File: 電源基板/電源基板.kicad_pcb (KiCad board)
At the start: 2 copper layers, 59.7 x 49.5 mm, 22 parts, among them J1 XT30, J2 PWR out, J3 Power Switch, J4 5V out, Q2 Q_NMOS_GDS, U1 OKL-T/6-W12N-C

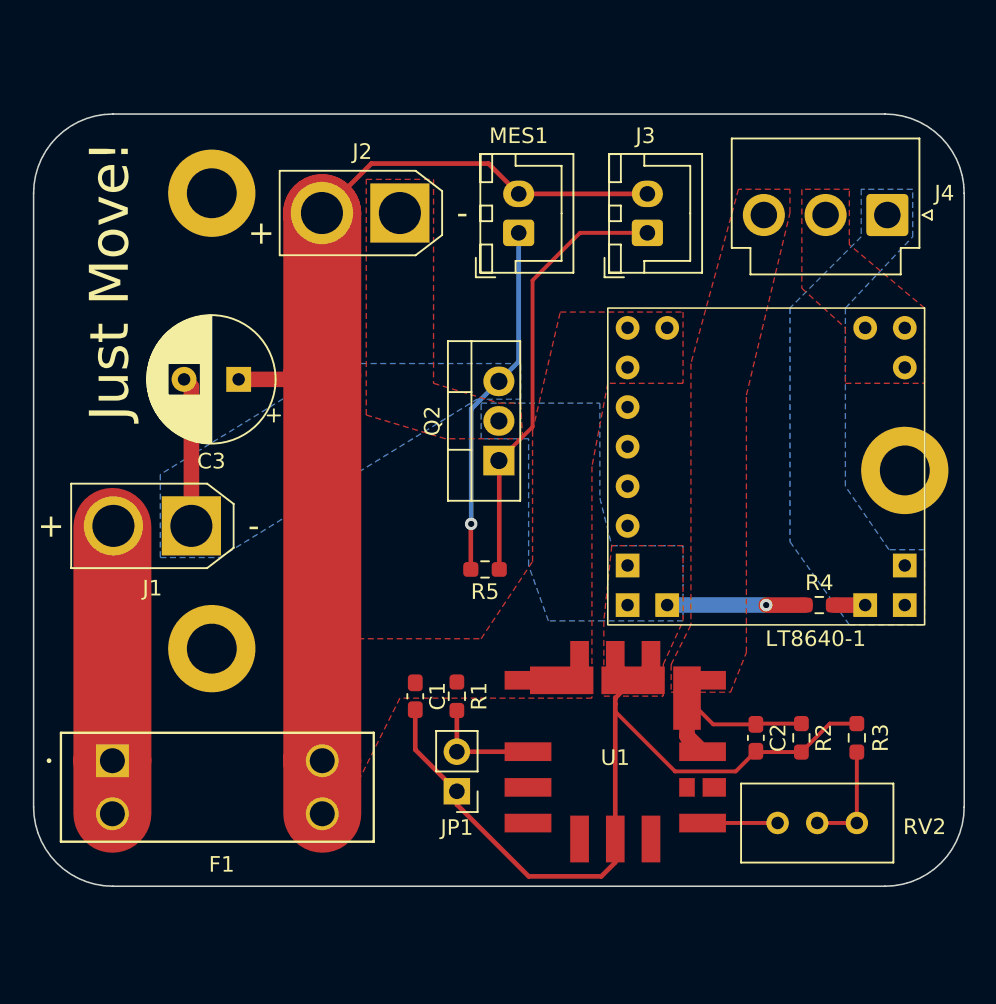
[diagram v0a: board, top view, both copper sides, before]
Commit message: パスコンと保護ダイオードの追加
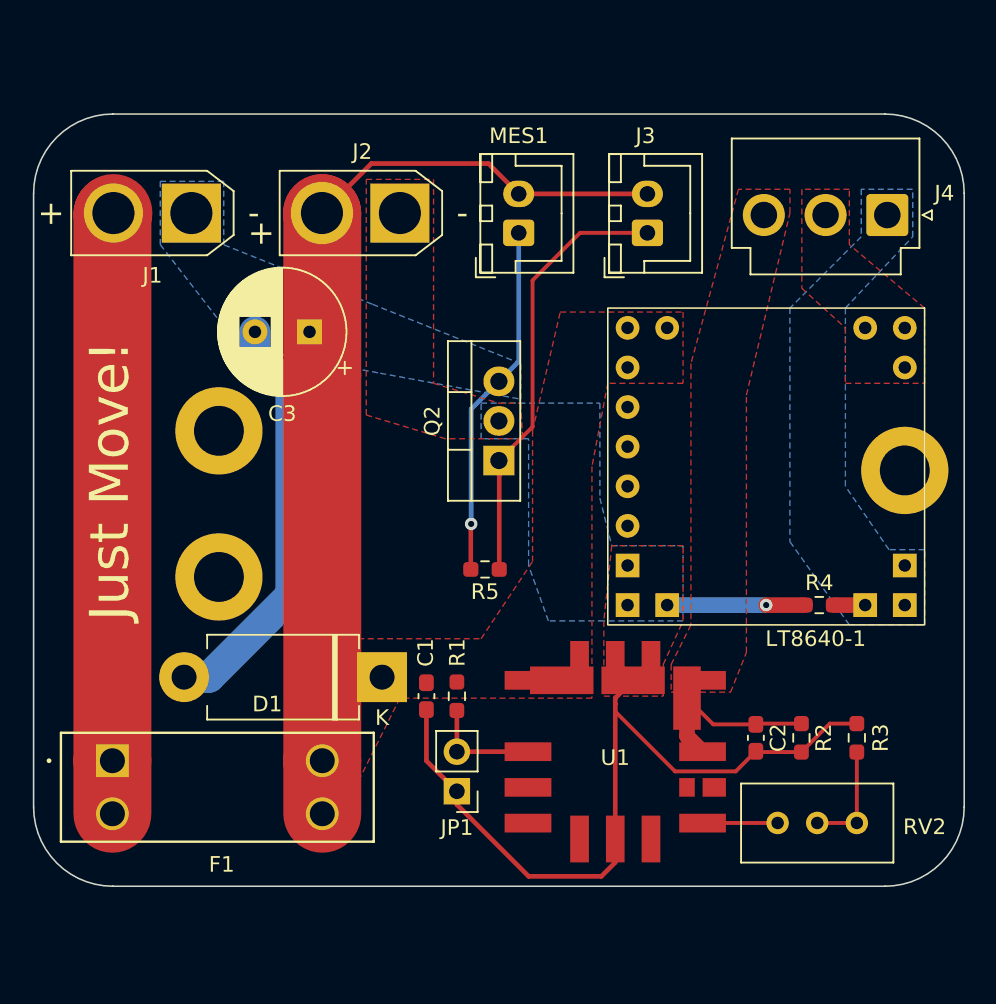
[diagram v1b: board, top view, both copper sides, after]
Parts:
- added D1: D_Shockley, Diode_THT:D_DO-201AD_P12.70mm_Horizontal, F.Cu at (52.8, 122.5)
- moved J1 20.1 mm to (40.6, 92.7)
- moved REF** 15.2 mm to (42.4, 106.7)
- moved C3 5.47 mm to (48.2, 100.3)
- moved REF** 4.62 mm to (42.4, 116.1)
- moved C1 0.71 mm to (55.7, 123.7)
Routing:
- net Net-(J1-Pin_2): track 18.6 -> 38.7 mm
- net GND: track 32.5 -> 49.7 mm
- net VDD: track 67.0 -> 61.5 mm

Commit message: サーボ基板
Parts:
- added J5: Conn_01x02_Pin, Connector_PinHeader_2.54mm:PinHeader_1x02_P2.54mm_Vertical, F.Cu at (53.0, 117.5)
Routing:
- net GND2: track 61.4 -> 77.2 mm

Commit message: 電源基板
白色にして発注
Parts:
- removed C1: 22u, Capacitor_SMD:C_0603_1608Metric_Pad1.08x0.95mm_HandSolder
- removed C2: 10u, Capacitor_SMD:C_0603_1608Metric_Pad1.08x0.95mm_HandSolder
- removed J5: Conn_01x02_Pin, Connector_PinHeader_2.54mm:PinHeader_1x02_P2.54mm_Vertical
- removed JP1: JumperShort, Connector_PinHeader_2.54mm:PinHeader_1x02_P2.54mm_Vertical
- removed R4: R_Small, Resistor_SMD:R_0603_1608Metric_Pad0.98x0.95mm_HandSolder
- removed the REF** at (42.4, 106.7)
- removed the REF** at (42.4, 116.1)
- removed the REF** at (86.4, 109.2)
- removed RV2: 20k, Potentiometer_THT:Potentiometer_Bourns_3296W_Vertical
- added D3: RED, LED_THT:LED_D5.0mm_Horizontal_O3.81mm_Z3.0mm, F.Cu at (79.8, 128.9)
- added FAN1: Conn_01x02_Pin, Connector_PinHeader_2.54mm:PinHeader_1x02_P2.54mm_Vertical, F.Cu at (65.2, 129.0)
- added G***: LOGO, logo:logo2, F.Cu at (33.0, 110.7)
- added LT8640-2: ~, LT8640:LT8640, F.Cu at (78.7, 122.7)
- added LT8640-3: ~, LT8640:LT8640, F.Cu at (78.7, 101.0)
- added REF**: MountingHole_2.2mm_M2_DIN965_Pad, MountingHole:MountingHole_2.2mm_M2_DIN965_Pad, F.Cu at (80.0, 101.0)
- added REF**: MountingHole_2.2mm_M2_DIN965_Pad, MountingHole:MountingHole_2.2mm_M2_DIN965_Pad, F.Cu at (80.3, 125.0)
- added REF**: MountingHole_2.2mm_M2_DIN965_Pad, MountingHole:MountingHole_2.2mm_M2_DIN965_Pad, F.Cu at (50.8, 107.3)
- J2: value PWR out -> Conn_01x02_Pin; footprint Connector_AMASS:AMASS_XT30U-F_1x02_P5.0mm_Vertical -> Connector_PinHeader_2.54mm:PinHeader_1x02_P2.54mm_Vertical
- J4: value 5V out -> PWR OUT; footprint Connector_JST:JST_VH_B3P-VH_1x03_P3.96mm_Vertical -> Connector_JST:JST_VH_B5P-VH_1x05_P3.96mm_Vertical
- R1: value 20k -> 220
- R2, R3: value 1.2k -> R_Small
- U1: value OKL-T/6-W12N-C -> ATtiny85-20P; footprint OKL-T_6-W12N-C:DCDC-murata-6A -> Package_DIP:DIP-8_W7.62mm
- moved MES1 37.0 mm to (59.8, 130.9), turned to 180 degrees
- moved R3 33.2 mm to (53.1, 112.7), turned to -90 degrees
- moved R2 31.7 mm to (51.2, 112.7), turned to 90 degrees
- moved J3 30.5 mm to (43.1, 108.7), turned to 180 degrees
- moved J2 30.0 mm to (57.1, 122.6), turned to 90 degrees
- moved U1 29.1 mm to (55.6, 104.9)
- moved R5 22.0 mm to (43.2, 100.7), turned to 90 degrees
- moved Q2 20.9 mm to (40.6, 101.6)
- moved LT8640-1 20.3 mm to (57.1, 109.9), turned to 180 degrees
- moved J4 20.3 mm to (64.9, 92.6)
- moved C3 16.4 mm to (44.0, 116.2)
- moved R1 7.65 mm to (65.3, 123.4), turned to 180 degrees
- moved J1 2.16 mm to (40.6, 90.6)
- moved D1 1.40 mm to (52.5, 123.8)
- moved F1 1.02 mm to (35.5, 128.9)
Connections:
- J2 pad 1: GND2 -> GND3
- J2 pad 2: VDD -> /tx
- J4 pad 1: GND2 -> GND3
- J4 pad 2: +5VA -> +5V
- J4 pad 3: +5VD -> GND1
- LT8640-1 pad 11: +5VA -> /6VA
- LT8640-1 pad 12: +5VA -> /6VA
- LT8640-1 pad 13: +5VA -> /6VA
- LT8640-1 pad 14: GND2 -> GND1
- LT8640-1 pad 15: GND2 -> GND1
- LT8640-1 pad 16: GND2 -> GND1
- LT8640-1 pad 4: unconnected-(LT8640-1-EN/UV-Pad4) -> /init_6v
- R1 pad 1: VDD -> Net-(D3-K)
- R1 pad 2: Net-(JP1-B) -> GND3
- R2 pad 1: +5VD -> VDD
- R2 pad 2: GND2 -> /Vref
- R3 pad 1: Net-(R3-Pad1) -> /Vref
- R3 pad 2: GND2 -> GND3
- U1 pad 1: Net-(JP1-B) -> unconnected-(U1-~{RESET}/PB5-Pad1)
- U1 pad 2: VDD -> /led
- U1 pad 3: GND2 -> /tx
- U1 pad 4: +5VD -> GND3
- U1 pad 5: +5VD -> /init_6v
- U1 pad 6: Net-(U1-TRIM1) -> /init_5v
- U1 pad 7: GND2 -> /Vref
- U1 pad 8: unconnected-(U1-NC-Pad8) -> +5V
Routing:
- net VDD: track 61.5 -> 152.4 mm
- net GND3: track 0.00 -> 78.0 mm, vias 0 -> 3
- net /6VB: track 0.00 -> 63.1 mm
- net /init_6v: track 0.00 -> 52.9 mm
- net GND1: track 0.00 -> 40.6 mm
- net /led: track 0.00 -> 38.9 mm, vias 0 -> 1
- net +5V: track 0.00 -> 36.4 mm
- net GND: track 49.7 -> 80.3 mm, vias 1 -> 0
- net /init_5v: track 0.00 -> 27.3 mm, vias 0 -> 1
- net Net-(J3-Pin_1): track 28.1 -> 10.7 mm
- net /6VA: track 0.00 -> 17.4 mm
- net Net-(D3-K): track 0.00 -> 15.8 mm
- net /Vref: track 0.00 -> 14.5 mm
- net /tx: track 0.00 -> 14.2 mm, vias 0 -> 2
- net +5VD: track 11.9 -> 0.00 mm
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- removed copper zone on F.Cu, net +5VA
- removed copper zone on F.Cu, net +5VD
- removed copper zone on B.Cu, net GND
- removed copper zone on F.Cu, net GND2
- removed copper zone on F.Cu, net VDD
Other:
- board text removed: "Just Move!"

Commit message: main
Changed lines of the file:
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@@
 		(tags "THT DIP DIL PDIP 2.54mm 7.62mm 300mil")
 		(property "Reference" "U1"
-			(at 3.8 10.15 360)
+			(at 3.8 10.15 0)
 			(layer "F.SilkS")
 			(effects
@@
 		)
 		(property "Value" "ATtiny85-20P"
-			(at 3.81 9.95 360)
+			(at 3.81 9.95 0)
 			(layer "F.Fab")
 			(effects
@@
 		)
 		(fp_text user "${REFERENCE}"
-			(at 3.81 3.81 360)
+			(at 3.81 3.81 0)
 			(layer "F.Fab")
 			(effects
@@
 		(tags "Diode DO-201AD series Axial Horizontal pin pitch 12.7mm  length 9.5mm diameter 5.2mm")
 		(property "Reference" "D1"
-			(at 6.223 3.429 360)
+			(at 6.223 3.429 0)
 			(layer "F.SilkS")
 			(effects
@@
 		)
 		(property "Value" "D_Shockley"
-			(at 6.35 3.72 360)
+			(at 6.35 3.72 0)
 			(layer "F.Fab")
 			(effects
@@
 		)
 		(fp_text user "K"
-			(at 0 -2.6 360)
+			(at 0 -2.6 0)
 			(layer "F.SilkS")
 			(effects
@@
 		)
 		(fp_text user "K"
-			(at 0 -2.6 360)
+			(at 0 -2.6 0)
 			(layer "F.Fab")
 			(effects
@@
 		)
 		(fp_text user "${REFERENCE}"
-			(at 7.0625 0 360)
+			(at 7.0625 0 0)
 			(layer "F.Fab")
 			(effects
@@
 		)
 		(property "Value" "Power Switch"
-			(at 1.25 4.6 360)
+			(at 1.25 4.6 0)
 			(layer "F.Fab")
 			(effects
@@
 		)
 		(fp_text user "${REFERENCE}"
-			(at 1.25 2.7 360)
+			(at 1.25 2.7 0)
 			(layer "F.Fab")
 			(effects
@@
 		)
 		(property "Value" "Voltmeter_DC_XH"
-			(at 1.25 4.6 360)
+			(at 1.25 4.6 0)
 			(layer "F.Fab")
 			(effects
@@
 		)
 		(fp_text user "${REFERENCE}"
-			(at 1.25 2.7 360)
+			(at 1.25 2.7 0)
 			(layer "F.Fab")
 			(effects
@@
 		(tags "resistor handsolder")
 		(property "Reference" "R1"
-			(at 0 -1.43 360)
+			(at 0 -1.43 0)
 			(layer "F.SilkS")
 			(effects
@@
 		)
 		(property "Value" "220"
-			(at 0 1.43 360)
+			(at 0 1.43 0)
 			(layer "F.Fab")
 			(effects
@@
 		)
 		(fp_text user "${REFERENCE}"
-			(at 0 0 360)
+			(at 0 0 0)
 			(layer "F.Fab")
 			(effects
@@
 		)
 		(property "Value" "1000u"
-			(at 1.75 5.25 360)
+			(at 1.75 5.25 0)
 			(layer "F.Fab")
 			(effects
@@
 		)
 		(fp_text user "${REFERENCE}"
-			(at 1.75 0 360)
+			(at 1.75 0 0)
 			(layer "F.Fab")
 			(effects
@@
 		(tags "connector JST VH vertical")
 		(property "Reference" "J4"
-			(at 7.92 -4.9 360)
+			(at 7.92 -4.9 0)
 			(layer "F.SilkS")
 			(effects
@@
 		)
 		(property "Value" "PWR OUT"
-			(at 7.92 6 360)
+			(at 7.92 6 0)
 			(layer "F.Fab")
 			(effects
@@
 		)
 		(fp_text user "${REFERENCE}"
-			(at 7.92 4.1 360)
+			(at 7.92 4.1 0)
 			(layer "F.Fab")
 			(effects
@@
 		)
 		(property "Footprint" "LT8640:LT8640"
-			(at 0 0 360)
+			(at 0 0 0)
 			(layer "F.Fab")
 			(hide yes)
@@
 		)
 		(property "Datasheet" ""
-			(at 0 0 360)
+			(at 0 0 0)
 			(layer "F.Fab")
 			(hide yes)
@@
 		)
 		(property "Description" ""
-			(at 0 0 360)
+			(at 0 0 0)
 			(layer "F.Fab")
 			(hide yes)
@@
 		)
 		(fp_text user "${REFERENCE}"
-			(at 0 1.27 360)
+			(at 0 1.27 0)
 			(layer "F.Fab")
 			(effects
@@
 		(at 33.02 110.744 90)
 		(property "Reference" "G***"
-			(at 0 0 90)
+			(at 0.254 -6.858 90)
 			(layer "F.SilkS")
+			(hide yes)
 			(effects
 				(font

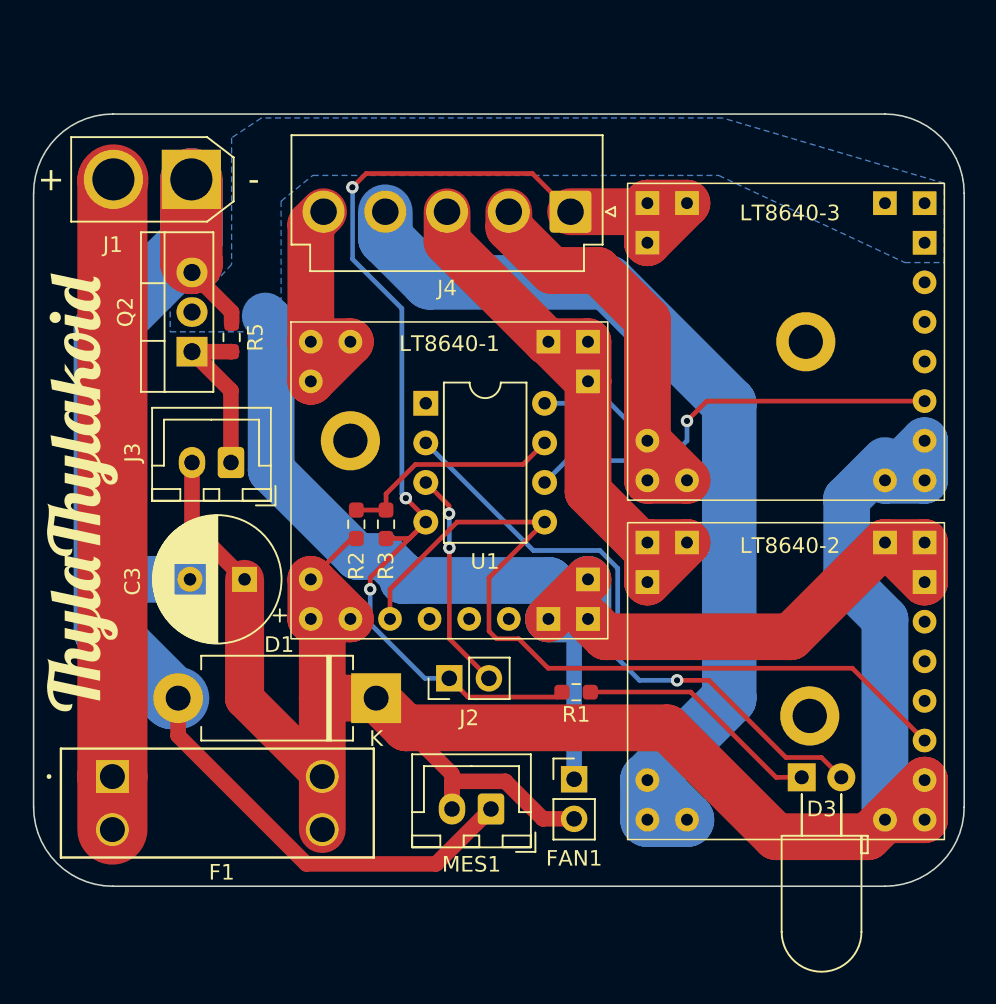
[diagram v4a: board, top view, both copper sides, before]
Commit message: 電源基板にATtiny用LDOを追加
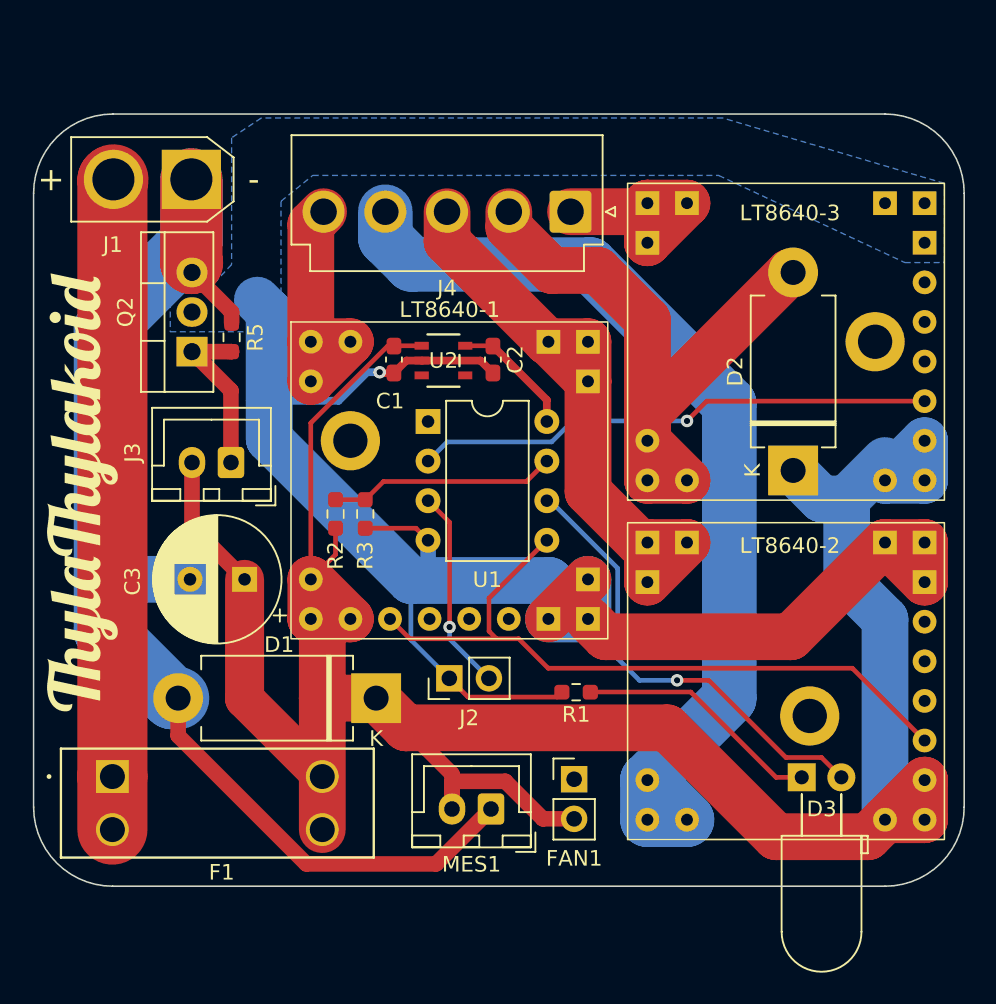
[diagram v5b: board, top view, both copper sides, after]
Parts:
- added C1: 0.1u, Capacitor_SMD:C_0603_1608Metric_Pad1.08x0.95mm_HandSolder, F.Cu at (53.6, 102.1)
- added C2: 0.47u, Capacitor_SMD:C_0603_1608Metric_Pad1.08x0.95mm_HandSolder, F.Cu at (59.9, 102.1)
- added D2: D_Shockley, Diode_THT:D_DO-201AD_P12.70mm_Horizontal, F.Cu at (79.2, 109.2)
- added U2: NJM12888F33-TE1, NJM12888:PI-SOT-23-5-E-A_NMD, F.Cu at (56.8, 102.2)
- F1: value 3557-15 -> 10A
- R2, R3: value R_Small -> 10k
- moved REF** 4.44 mm to (84.5, 101.0)
- moved R2 1.49 mm to (49.8, 112.0)
- moved R3 1.49 mm to (51.8, 112.0)
- moved U1 1.18 mm to (55.8, 106.1)
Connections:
- net /Vref renamed Net-(U1-PB2)
- C3 pad 2: GND -> Net-(D1-A)
- D1 pad 2: GND -> Net-(D1-A)
- J1 pad 1: GND -> Net-(D1-A)
- J2 pad 1: GND3 -> GND
- LT8640-1 pad 10: GND2 -> GND
- LT8640-1 pad 8: GND2 -> GND
- LT8640-1 pad 9: GND2 -> GND
- LT8640-2 pad 10: GND2 -> GND
- LT8640-2 pad 8: GND2 -> GND
- LT8640-2 pad 9: GND2 -> GND
- LT8640-3 pad 10: GND2 -> GND
- LT8640-3 pad 8: GND2 -> GND
- LT8640-3 pad 9: GND2 -> GND
- MES1 pad 1: GND -> Net-(D1-A)
- Q2 pad 2: GND2 -> GND
- Q2 pad 3: GND -> Net-(D1-A)
- R1 pad 2: GND3 -> GND
- R3 pad 2: GND3 -> GND
- R5 pad 2: GND -> Net-(D1-A)
- U1 pad 2: /led -> /init_5v
- U1 pad 4: GND3 -> GND
- U1 pad 6: /init_5v -> /led
- U1 pad 8: +5V -> +5VA
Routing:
- net GND2: track 84.5 -> 0.00 mm
- net Net-(D1-A): track 0.00 -> 80.3 mm
- net GND3: track 78.0 -> 13.8 mm, vias 3 -> 0
- net GND: track 80.3 -> 112.1 mm, vias 0 -> 1
- net VDD: track 152.4 -> 175.8 mm
- net /led: track 38.9 -> 29.6 mm
- net +5VA: track 0.00 -> 8.05 mm
- net /init_6v: track 52.9 -> 45.6 mm
- net +5V: track 36.4 -> 43.6 mm
- net /init_5v: track 27.3 -> 33.4 mm
- net /tx: track 14.2 -> 13.0 mm, vias 2 -> 1
- added copper zone on B.Cu, net GND
- removed copper zone on B.Cu, net GND2
